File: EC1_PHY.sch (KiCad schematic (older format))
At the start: 72 parts

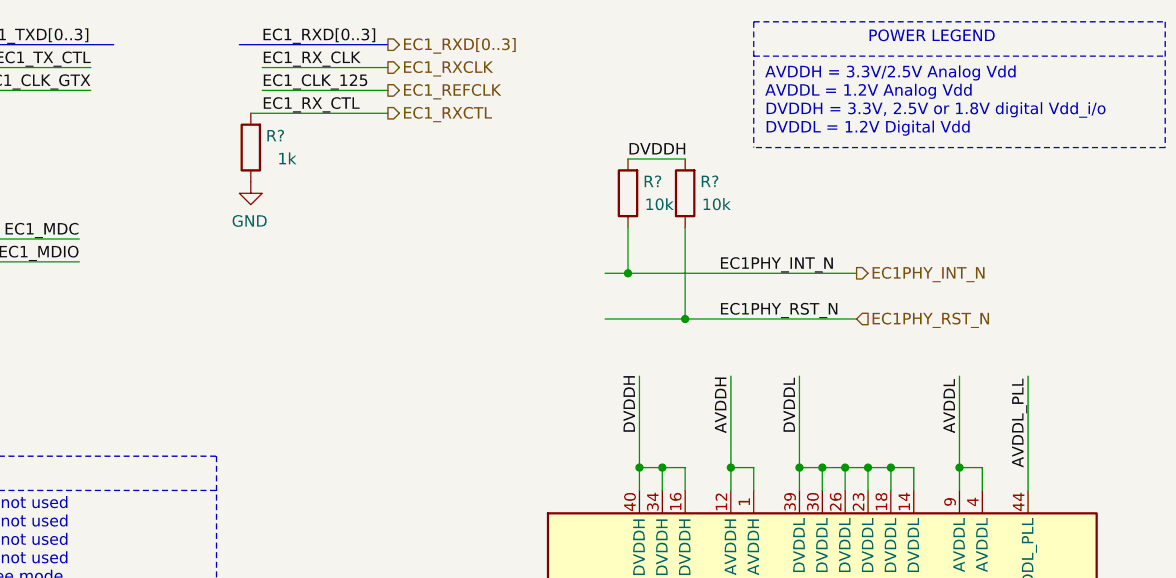
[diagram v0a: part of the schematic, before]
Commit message: Fix reset signal path
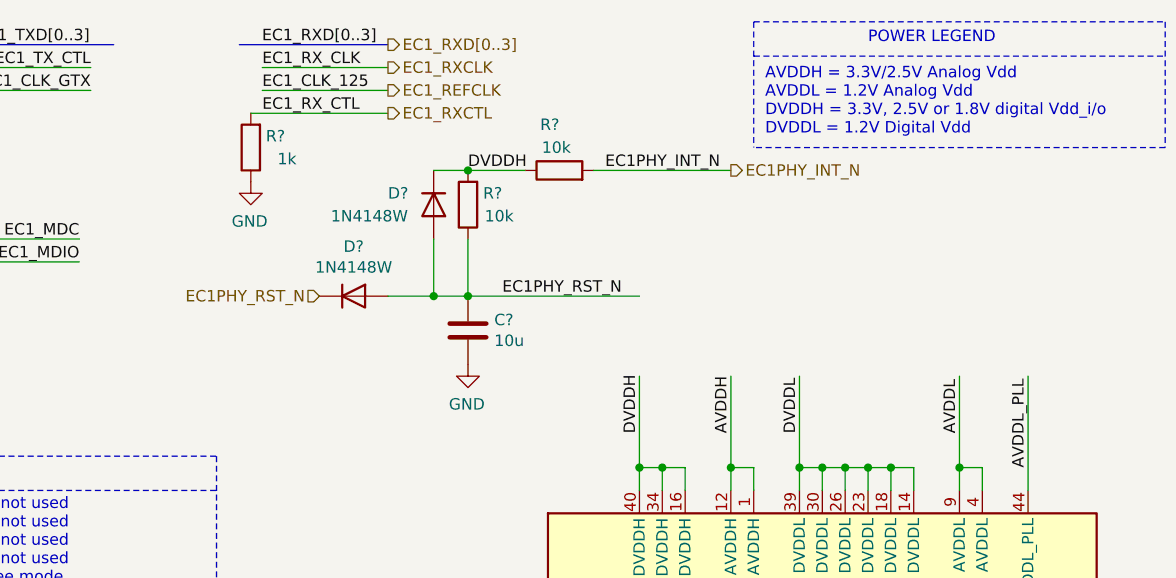
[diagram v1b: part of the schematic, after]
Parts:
- added C?: 10u, symbol Device:C
- added D? (x2): 1N4148W, Diode_SMD:D_SOD-123, symbol Diode:1N4148W
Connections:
- wire segments 220 -> 221
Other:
- moved on the sheet: R?
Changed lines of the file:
@@
 Text Label 3000 5050 0    50   ~ 0
 EC1PHY_INT_N
-Text Label 4450 1600 0    50   ~ 0
+Text Label 3950 1150 0    50   ~ 0
 EC1PHY_INT_N
-Text HLabel 5050 1600 2    50   Output ~ 0
+Text HLabel 4500 1150 2    50   Output ~ 0
 EC1PHY_INT_N
 Text Label 3000 5350 0    50   ~ 0
@@
 L Device:R R?
 U 1 1 5FF1CC7D
-P 4050 1250
+P 3750 1150
 AR Path="/5FC823B8/5FF1CC7D" Ref="R?"  Part="1"
 AR Path="/5FD29175/5FF1CC7D" Ref="R?"  Part="1"
 AR Path="/60A03338/5FF1CC7D" Ref="R?"  Part="1"
-F 0 "R?" H 3900 1200 50  0000 L CNN
-F 1 "10k" H 3850 1300 50  0000 L CNN
-F 2 "" V 3980 1250 50  0001 C CNN
-F 3 "~" H 4050 1250 50  0001 C CNN
-	1    4050 1250
-	-1   0    0    1
+F 0 "R?" V 3950 1150 50  0000 L CNN
+F 1 "10k" V 3850 1100 50  0000 L CNN
+F 2 "" V 3680 1150 50  0001 C CNN
+F 3 "~" H 3750 1150 50  0001 C CNN
+	1    3750 1150
+	0    -1   -1   0
 $EndComp
 $Comp
 L Device:R R?
 U 1 1 5FF1CC8B
-P 4300 1250
+P 3350 1300
 AR Path="/5FC823B8/5FF1CC8B" Ref="R?"  Part="1"
 AR Path="/5FD29175/5FF1CC8B" Ref="R?"  Part="1"
 AR Path="/60A03338/5FF1CC8B" Ref="R?"  Part="1"
-F 0 "R?" H 4150 1200 50  0000 L CNN
-F 1 "10k" H 4100 1300 50  0000 L CNN
-F 2 "" V 4230 1250 50  0001 C CNN
-F 3 "~" H 4300 1250 50  0001 C CNN
-	1    4300 1250
+F 0 "R?" H 3200 1250 50  0000 L CNN
+F 1 "10k" H 3150 1350 50  0000 L CNN
+F 2 "" V 3280 1300 50  0001 C CNN
+F 3 "~" H 3350 1300 50  0001 C CNN
+	1    3350 1300
 	-1   0    0    1
 $EndComp
 Wire Wire Line
-	4300 1100 4050 1100
+	3600 1150 3350 1150
 Wire Wire Line
 	3000 5350 3600 5350
 Wire Wire Line
 	3000 5050 3600 5050
-Text Label 4450 1800 0    50   ~ 0
+Text Label 3500 1700 0    50   ~ 0
 EC1PHY_RST_N
-Text HLabel 5050 1800 2    50   Input ~ 0
+Text HLabel 2700 1700 0    50   Input ~ 0
 EC1PHY_RST_N
 Wire Wire Line
-	3950 1600 4050 1600
-Wire Wire Line
-	3950 1800 4300 1800
-Wire Wire Line
-	4050 1400 4050 1600
-Connection ~ 4050 1600
-Wire Wire Line
-	4050 1600 5050 1600
-Wire Wire Line
-	4300 1400 4300 1800
-Connection ~ 4300 1800
-Wire Wire Line
-	4300 1800 5050 1800
+	3000 1700 3200 1700
+Wire Wire Line
+	3900 1150 4500 1150
+Wire Wire Line
+	3350 1450 3350 1700
+Connection ~ 3350 1700
+Wire Wire Line
+	3350 1700 4100 1700
 Text Label 10600 2200 0    50   ~ 0
 AVDDL
@@
 Text Label 8500 2950 0    50   ~ 0
 DVDDH
-Text Label 4050 1100 0    50   ~ 0
+Text Label 3350 1150 0    50   ~ 0
 DVDDH
 Text Label 4100 2300 1    50   ~ 0
@@
 Text Label 2650 3250 0    50   ~ 0
 EC1_MDIO
+$Comp
+L Device:C C?
+U 1 1 6052658F
+P 3350 1850
+AR Path="/5FC823B8/6052658F" Ref="C?"  Part="1"
+AR Path="/5FD29175/6052658F" Ref="C?"  Part="1"
+AR Path="/60A03338/6052658F" Ref="C?"  Part="1"
+F 0 "C?" H 3465 1896 50  0000 L CNN
+F 1 "10u" H 3465 1805 50  0000 L CNN
+F 2 "" H 3388 1700 50  0001 C CNN
+F 3 "~" H 3350 1850 50  0001 C CNN
+	1    3350 1850
+	1    0    0    -1
+$EndComp
+$Comp
+L power:GND #PWR?
+U 1 1 60536F5C
+P 3350 2000
+AR Path="/5FC823B8/60536F5C" Ref="#PWR?"  Part="1"
+AR Path="/5FD29175/60536F5C" Ref="#PWR?"  Part="1"
+AR Path="/60A03338/60536F5C" Ref="#PWR?"  Part="1"
+F 0 "#PWR?" H 3350 1750 50  0001 C CNN
+F 1 "GND" H 3355 1827 50  0000 C CNN
+F 2 "" H 3350 2000 50  0001 C CNN
+F 3 "" H 3350 2000 50  0001 C CNN
+	1    3350 2000
+	-1   0    0    -1
+$EndComp
+$Comp
+L Diode:1N4148W D?
+U 1 1 6060D249
+P 3200 1300
+F 0 "D?" V 3150 1100 50  0000 L CNN
+F 1 "1N4148W" V 3250 850 50  0000 L CNN
+F 2 "Diode_SMD:D_SOD-123" H 3200 1125 50  0001 C CNN
+F 3 "https://www.vishay.com/docs/85748/1n4148w.pdf" H 3200 1300 50  0001 C CNN
+	1    3200 1300
+	0    1    1    0
+$EndComp
+$Comp
+L Diode:1N4148W D?
+U 1 1 60640C58
+P 2850 1700
+F 0 "D?" H 2850 1917 50  0000 C CNN
+F 1 "1N4148W" H 2850 1826 50  0000 C CNN
+F 2 "Diode_SMD:D_SOD-123" H 2850 1525 50  0001 C CNN
+F 3 "https://www.vishay.com/docs/85748/1n4148w.pdf" H 2850 1700 50  0001 C CNN
+	1    2850 1700
+	1    0    0    -1
+$EndComp
+Wire Wire Line
+	3200 1450 3200 1700
+Connection ~ 3200 1700
+Wire Wire Line
+	3200 1700 3350 1700
+Wire Wire Line
+	3200 1150 3350 1150
+Connection ~ 3350 1150
 $EndSCHEMATC
